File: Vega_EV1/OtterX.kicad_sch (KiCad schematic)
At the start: 74 parts, among them J1 VERA_CONN, J11 KMDGX-6SG, J12 VIA1 Extra Pins, J17 SNES23, J18 SNES0, J19 SNES1, J2 VIA2 Header, J29 AudioPlug3, J3 ISP, J9 I2C, U1 W65C02S, U11 74ACT163, U2 W65C22S, U3 74LS06, X1 ACH-16.000MHZ-EK

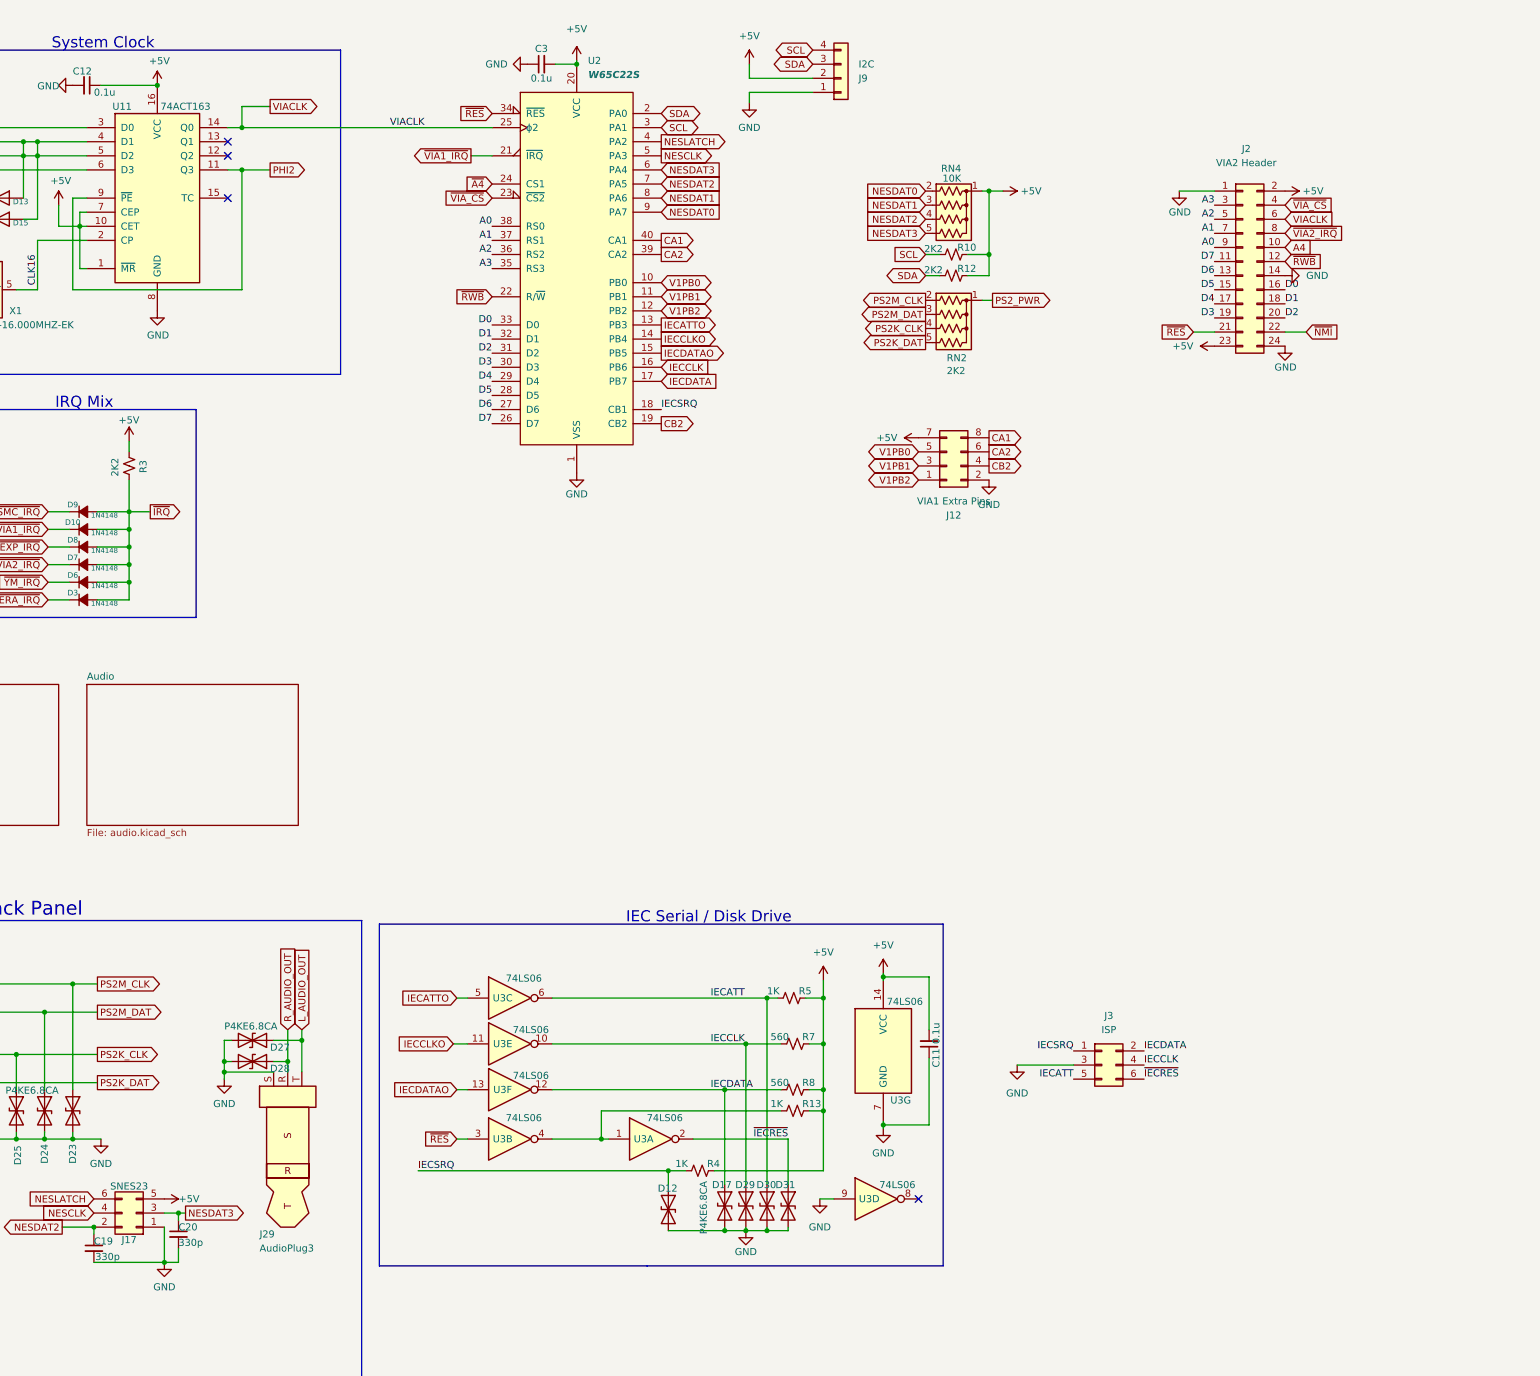
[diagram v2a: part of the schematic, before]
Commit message: More space between Edge and YM2151 Add IEC logic back in IDC headers for NES and IEC
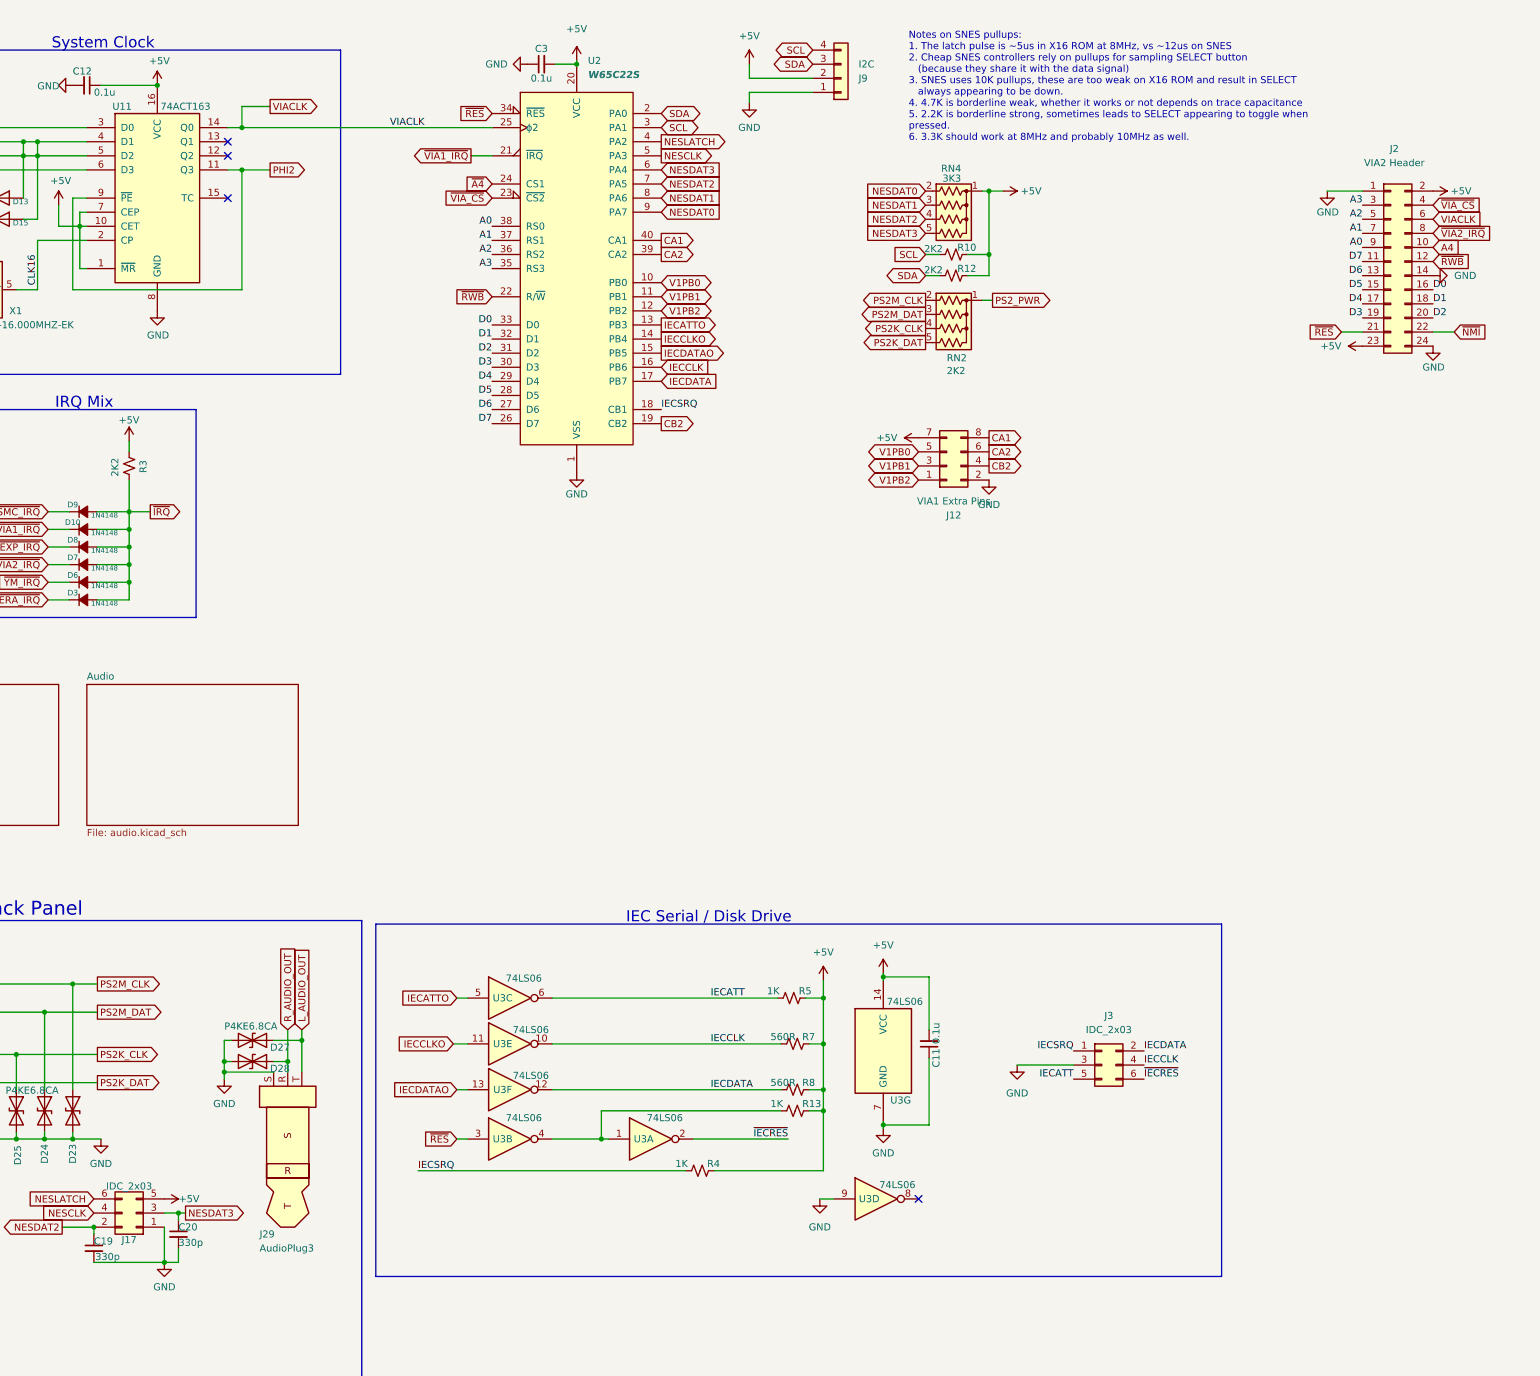
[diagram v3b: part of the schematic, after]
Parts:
- removed D12, D17, D29, D30, D31: P4KE6.8CA, Diode_THT:D_DO-41_SOD81_P7.62mm_Horizontal, symbol Device:D_TVS
- D13, D15: footprint Diode_THT:D_DO-35_SOD27_P7.62mm_Horizontal -> Diode_THT:D_DO-34_SOD68_P7.62mm_Horizontal
- J17: value SNES23 -> IDC_2x03
- J3: value ISP -> IDC_2x03
- R3: footprint Resistor_THT:R_Axial_DIN0207_L6.3mm_D2.5mm_P10.16mm_Horizontal -> Resistor_THT:R_Axial_DIN0207_L6.3mm_D2.5mm_P7.62mm_Horizontal
- R7, R8: value 560 -> 560R
- RN4: value 10K -> 3K3
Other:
- note added: "Notes on SNES pullups: 1. The latch pulse is ~5us in X16 ROM at 8MHz, vs ~12us on SNES 2. Cheap SNES controllers rely on pullups for sampling SELECT button (because they share it with the data signal) 3. SNES uses 10K pullups, these are too weak on X16 ROM and result in SELECT always appearing to be down. 4. 4.7K is borderline weak, whether it works or not depends on trace capacitance 5. 2.2K is 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"
- moved on the sheet: J2

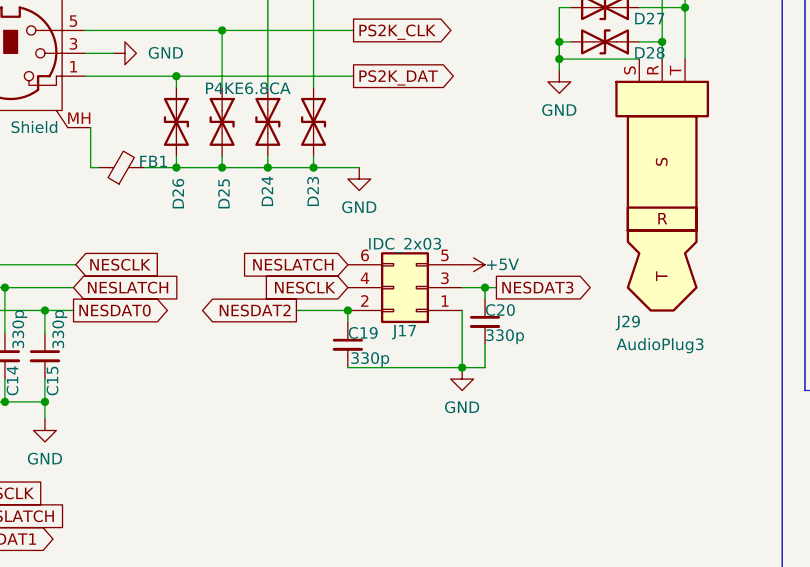
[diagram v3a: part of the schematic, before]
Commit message: Add dongle boards and new battery clip
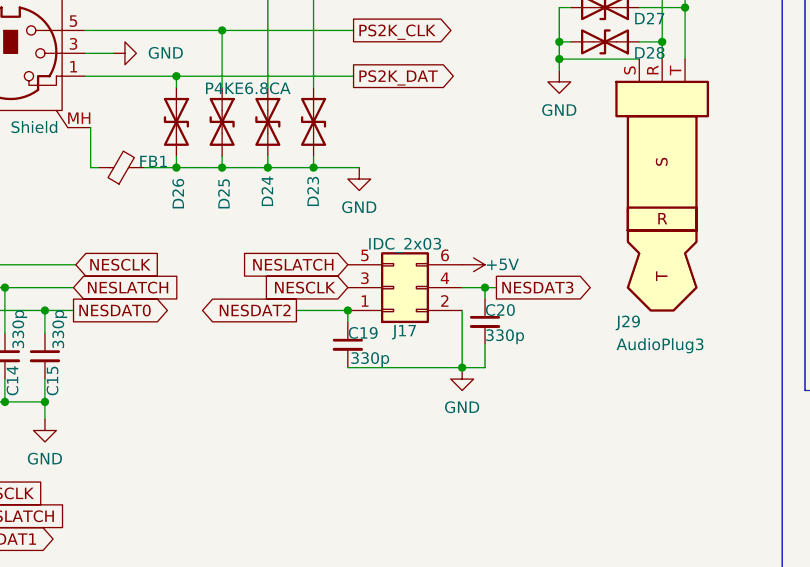
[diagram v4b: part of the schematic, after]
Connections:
- net +5V: now also J17.6 (Pin_6); no longer J17.5 (Pin_5)
- net GND: now also J17.2 (Pin_2); no longer J17.1 (Pin_1)
- net NESCLK: now also J17.3 (Pin_3); no longer J17.4 (Pin_4)
- net NESDAT2: now also J17.1 (Pin_1); no longer J17.2 (Pin_2)
- net NESDAT3: now also J17.4 (Pin_4); no longer J17.3 (Pin_3)
- net NESLATCH: now also J17.5 (Pin_5); no longer J17.6 (Pin_6)
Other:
- moved on the sheet: J17
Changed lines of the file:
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@@
 	(symbol
 		(lib_id "Connector_Generic:Conn_02x03_Odd_Even")
-		(at 158.75 229.87 180)
+		(at 156.21 229.87 0)
+		(mirror x)
 		(unit 1)
 		(exclude_from_sim no)
@@
 		)
 		(property "Footprint" "Connector_IDC:IDC-Header_2x03_P2.54mm_Vertical"
-			(at 158.75 229.87 0)
+			(at 156.21 229.87 0)
 			(effects
 				(font
@@
 		)
 		(property "Datasheet" "~"
-			(at 158.75 229.87 0)
+			(at 156.21 229.87 0)
 			(effects
 				(font
@@
 		)
 		(property "Description" ""
-			(at 158.75 229.87 0)
+			(at 156.21 229.87 0)
 			(effects
 				(font

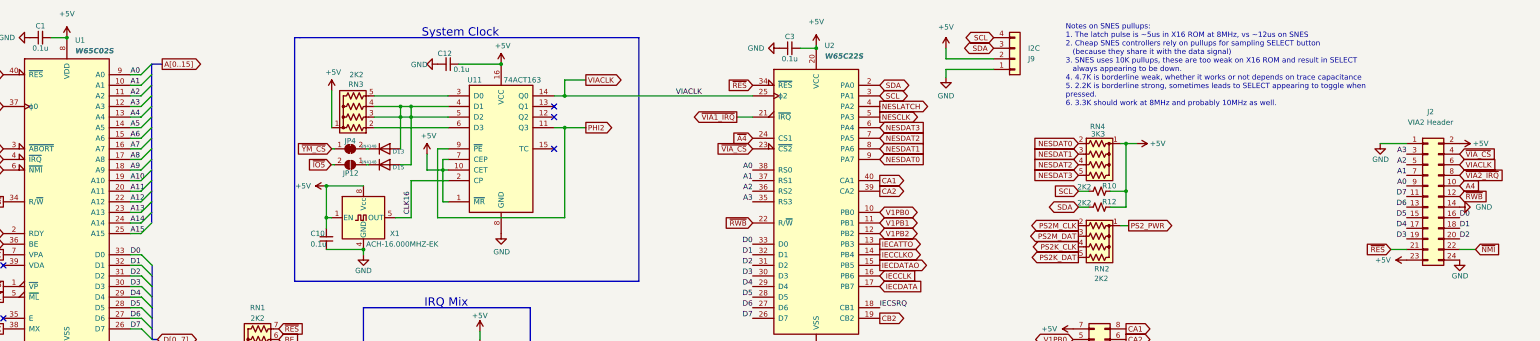
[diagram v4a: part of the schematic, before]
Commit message: Change 2.2u cap footprint; update MemoryExpansion
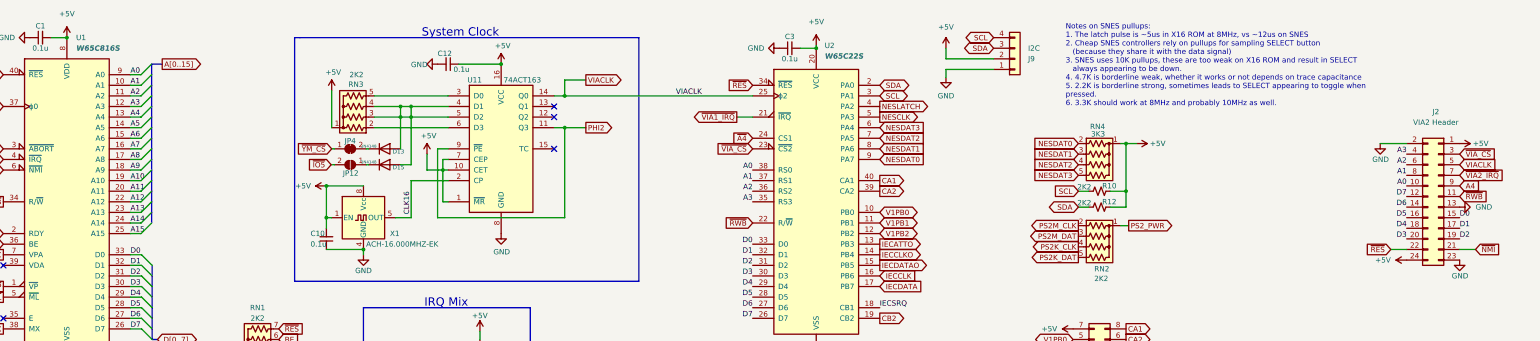
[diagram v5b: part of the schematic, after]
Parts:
- J2: footprint Connector_PinSocket_2.54mm:PinSocket_2x12_P2.54mm_Vertical -> Connector_PinHeader_2.54mm:PinHeader_2x12_P2.54mm_Vertical
- U1: value W65C02S -> W65C816S
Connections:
- net +5V: now also J2.1 (Pin_1), J2.24 (Pin_24); no longer J2.2 (Pin_2), J2.23 (Pin_23)
- net A0: now also J2.10 (Pin_10); no longer J2.9 (Pin_9)
- net A1: now also J2.8 (Pin_8); no longer J2.7 (Pin_7)
- net A2: now also J2.6 (Pin_6); no longer J2.5 (Pin_5)
- net A3: now also J2.4 (Pin_4); no longer J2.3 (Pin_3)
- net A4: now also J2.9 (Pin_9); no longer J2.10 (Pin_10)
- net D0: now also J2.15 (Pin_15); no longer J2.16 (Pin_16)
- net D1: now also J2.17 (Pin_17); no longer J2.18 (Pin_18)
- net D2: now also J2.19 (Pin_19); no longer J2.20 (Pin_20)
- net D3: now also J2.20 (Pin_20); no longer J2.19 (Pin_19)
- net D4: now also J2.18 (Pin_18); no longer J2.17 (Pin_17)
- net D5: now also J2.16 (Pin_16); no longer J2.15 (Pin_15)
- net D6: now also J2.14 (Pin_14); no longer J2.13 (Pin_13)
- net D7: now also J2.12 (Pin_12); no longer J2.11 (Pin_11)
- net GND: now also J2.13 (Pin_13), J2.2 (Pin_2), J2.23 (Pin_23); no longer J2.1 (Pin_1), J2.14 (Pin_14), J2.24 (Pin_24)
- net VIACLK: now also J2.5 (Pin_5); no longer J2.6 (Pin_6)
- net ~{NMI}: now also J2.21 (Pin_21); no longer J2.22 (Pin_22)
- net ~{RES}: now also J2.22 (Pin_22); no longer J2.21 (Pin_21)
- net ~{RWB}: now also J2.11 (Pin_11); no longer J2.12 (Pin_12)
- net ~{VIA2_IRQ}: now also J2.7 (Pin_7); no longer J2.8 (Pin_8)
- net ~{VIA_CS}: now also J2.3 (Pin_3); no longer J2.4 (Pin_4)
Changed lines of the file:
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@@
 	(symbol
 		(lib_id "Connector_Generic:Conn_02x12_Odd_Even")
-		(at 384.81 58.42 0)
+		(at 387.35 58.42 0)
+		(mirror y)
 		(unit 1)
 		(exclude_from_sim no)
@@
 		(dnp no)
 		(property "Reference" "J2"
-			(at 385.445 38.1 0)
+			(at 386.715 38.1 0)
 			(effects
 				(font
@@
 		)
 		(property "Value" "VIA2 Header"
-			(at 385.445 40.64 0)
-			(effects
-				(font
-					(size 1.27 1.27)
-				)
-			)
-		)
-		(property "Footprint" "Connector_PinSocket_2.54mm:PinSocket_2x12_P2.54mm_Vertical"
-			(at 384.81 58.42 0)
+			(at 386.715 40.64 0)
+			(effects
+				(font
+					(size 1.27 1.27)
+				)
+			)
+		)
+		(property "Footprint" "Connector_PinHeader_2.54mm:PinHeader_2x12_P2.54mm_Vertical"
+			(at 387.35 58.42 0)
 			(effects
 				(font
@@
 		)
 		(property "Datasheet" "~"
-			(at 384.81 58.42 0)
+			(at 387.35 58.42 0)
 			(effects
 				(font
@@
 		)
 		(property "Description" ""
-			(at 384.81 58.42 0)
+			(at 387.35 58.42 0)
 			(effects
 				(font
@@
 		(fields_autoplaced yes)
 		(property "Reference" "U1"
-			(at 60.3759 20.955 0)
-			(effects
-				(font
-					(size 1.27 1.27)
-				)
-				(justify left)
-			)
-		)
-		(property "Value" "W65C02S"
-			(at 60.3759 23.495 0)
-			(effects
-				(font
+			(at 60.6141 20.32 0)
+			(effects
+				(font
+					(size 1.27 1.27)
+				)
+				(justify left)
+			)
+		)
+		(property "Value" "W65C816S"
+			(at 60.6141 22.86 0)
+			(effects
+				(font
